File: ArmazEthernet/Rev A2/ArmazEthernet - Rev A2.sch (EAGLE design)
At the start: 114 parts, among them J1 22-05-7028-02, P1 RB1-125BAG1A, U1 LM317MDCY, U2 LM317MDCY, U3 KSZ8995MA, U4 AT24C02C-SSHM-B, X1 NE8FAV, X2 NE8FAV, Y1 8Z-25.000MHZMAAJ-T

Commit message: Update the board with the update schematic
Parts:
- added LED4, LED5, LED6, LED7: Blue, led:LEDCHIP-LED0603
- added R41, R42, R43, R44: 1k, rcl:R-EU_R0603
- JP2, JP3, JP4, JP5: device pinhead:PINHD-1X6 -> pinhead:PINHD-1X8
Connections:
- new net L1-1: JP2.7, JP3.7, R41.2
- new net L1-2: JP2.6, JP3.6, R42.2
- new net L2-1: JP4.7, JP5.7, R43.2
- new net L2-2: JP4.6, JP5.6, R44.2
- new net N$20: LED4.A, R41.1
- new net N$28: LED5.A, R42.1
- new net N$29: LED6.A, R43.1
- new net N$30: LED7.A, R44.1
- net GND: now also JP2.8, JP3.8, JP4.8, JP5.8, LED4.C, LED5.C, LED6.C, LED7.C; no longer JP2.6, JP3.6, JP4.6, JP5.6
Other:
- moved on the sheet: C11, C13, C14, C16, R12, R13, R14, R15, R16, R23, R24, R25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

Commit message: Update board and change NC to DNI
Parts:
- removed R32, R33: 0, NC, rcl:R-EU_R0603
- R30, R31: value 10K -> 10K, DNI
- R35, R36, R37, R38, R39, R40: value 0, NC -> 0, DNI
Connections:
- net N$21 renamed +3V3/FIL
- net N$22 renamed +1V8/FIL
- removed net N$25: R30.1, R32.2
- removed net N$27: R31.1, R33.2
- net L1-1: now also JP2.6, JP3.6, U3B.LED1-0; no longer JP2.7, JP3.7
- net L1-2: now also JP2.7, JP3.7, U3B.LED1-1; no longer JP2.6, JP3.6
- net L2-1: now also JP4.6, JP5.6, U3B.LED2-0; no longer JP4.7, JP5.7
- net L2-2: now also JP4.7, JP5.7, U3B.LED2-1; no longer JP4.6, JP5.6
- net PS0: now also R31.1; no longer R33.1
- net PS1: now also R30.1; no longer R32.1
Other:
- note added: "If CPU Interface controle Mode: Connect R30 Else: Do not connect R30 and R31"
- note removed: "If CPU Interface controle Mode: Connect R32"

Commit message: Update the board
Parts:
- added SJ1: (no value), jumper:SJ
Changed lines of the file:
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@@
 <part name="GND36" library="supply1" deviceset="GND" device=""/>
 <part name="GND37" library="supply1" deviceset="GND" device=""/>
+<part name="SJ1" library="jumper" deviceset="SJ" device=""/>
 </parts>
 <sheets>
@@
 <instance part="GND36" gate="1" x="20.32" y="7.62"/>
 <instance part="GND37" gate="1" x="10.16" y="7.62"/>
+<instance part="SJ1" gate="1" x="63.5" y="167.64"/>
 </instances>
 <busses>

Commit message: Board all route
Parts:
- removed C33: 0.1uF, rcl:C-EUC0603
- removed SJ1: (no value), jumper:SJ
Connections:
- net +1V8: no longer C32.1, C33.1
- net +3V3: now also C32.1
- net GND: no longer C33.2
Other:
- moved on the sheet: C32, C34, C35, C36
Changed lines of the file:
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@@
 <part name="C31" library="rcl" deviceset="C-EU" device="C0603" value="0.1uF"/>
 <part name="C32" library="rcl" deviceset="C-EU" device="C0603" value="0.1uF"/>
-<part name="C33" library="rcl" deviceset="C-EU" device="C0603" value="0.1uF"/>
 <part name="C34" library="rcl" deviceset="C-EU" device="C0603" value="0.1uF"/>
 <part name="C35" library="rcl" deviceset="C-EU" device="C0603" value="0.1uF"/>
@@
 <part name="GND36" library="supply1" deviceset="GND" device=""/>
 <part name="GND37" library="supply1" deviceset="GND" device=""/>
-<part name="SJ1" library="jumper" deviceset="SJ" device=""/>
 </parts>
 <sheets>
@@
 <instance part="GND36" gate="1" x="20.32" y="7.62"/>
 <instance part="GND37" gate="1" x="10.16" y="7.62"/>
-<instance part="SJ1" gate="1" x="63.5" y="167.64"/>
 </instances>
 <busses>
@@
 <text x="358.14" y="246.38" size="1.6764" layer="94">VDDIO</text>
 <text x="335.28" y="246.38" size="1.6764" layer="94">VDDAT</text>
-<text x="335.28" y="220.98" size="1.6764" layer="94">VDDAR</text>
+<text x="342.9" y="220.98" size="1.6764" layer="94">VDDAR</text>
 <text x="358.14" y="198.12" size="1.6764" layer="94">VDDC</text>
 <text x="335.28" y="198.12" size="1.6764" layer="94">VDDAP</text>
@@
 <instance part="C30" gate="G$1" x="340.36" y="241.3"/>
 <instance part="C31" gate="G$1" x="373.38" y="215.9"/>
-<instance part="C32" gate="G$1" x="365.76" y="215.9"/>
-<instance part="C33" gate="G$1" x="358.14" y="215.9"/>
-<instance part="C34" gate="G$1" x="350.52" y="215.9"/>
-<instance part="C35" gate="G$1" x="342.9" y="215.9"/>
-<instance part="C36" gate="G$1" x="335.28" y="215.9"/>
+<instance part="C32" gate="G$1" x="332.74" y="241.3"/>
+<instance part="C34" gate="G$1" x="365.76" y="215.9"/>
+<instance part="C35" gate="G$1" x="358.14" y="215.9"/>
+<instance part="C36" gate="G$1" x="350.52" y="215.9"/>
 <instance part="C37" gate="G$1" x="347.98" y="193.04"/>
 <instance part="C38" gate="G$1" x="373.38" y="193.04"/>
@@
 <wire x1="347.98" y1="236.22" x2="340.36" y2="236.22" width="0.1524" layer="91"/>
 <junction x="347.98" y="236.22"/>
-</segment>
-<segment>
+<pinref part="C32" gate="G$1" pin="2"/>
+<wire x1="340.36" y1="236.22" x2="332.74" y2="236.22" width="0.1524" layer="91"/>
+<junction x="340.36" y="236.22"/>
+</segment>
+<segment>
+<pinref part="C31" gate="G$1" pin="2"/>
 <pinref part="GND24" gate="1" pin="GND"/>
-<pinref part="C31" gate="G$1" pin="2"/>
 <wire x1="373.38" y1="208.28" x2="373.38" y2="210.82" width="0.1524" layer="91"/>
-<pinref part="C32" gate="G$1" pin="2"/>
-<wire x1="373.38" y1="210.82" x2="365.76" y2="210.82" width="0.1524" layer="91"/>
+<pinref part="C36" gate="G$1" pin="2"/>
+<pinref part="C35" gate="G$1" pin="2"/>
+<junction x="358.14" y="210.82"/>
+<wire x1="365.76" y1="210.82" x2="358.14" y2="210.82" width="0.1524" layer="91"/>
+<wire x1="358.14" y1="210.82" x2="350.52" y2="210.82" width="0.1524" layer="91"/>
+<pinref part="C34" gate="G$1" pin="2"/>
+<junction x="365.76" y="210.82"/>
+<wire x1="365.76" y1="210.82" x2="373.38" y2="210.82" width="0.1524" layer="91"/>
 <junction x="373.38" y="210.82"/>
-<pinref part="C33" gate="G$1" pin="2"/>
-<wire x1="365.76" y1="210.82" x2="358.14" y2="210.82" width="0.1524" layer="91"/>
-<junction x="365.76" y="210.82"/>
-<pinref part="C36" gate="G$1" pin="2"/>
-<wire x1="358.14" y1="210.82" x2="350.52" y2="210.82" width="0.1524" layer="91"/>
-<junction x="358.14" y="210.82"/>
-<pinref part="C35" gate="G$1" pin="2"/>
-<junction x="342.9" y="210.82"/>
-<wire x1="350.52" y1="210.82" x2="342.9" y2="210.82" width="0.1524" layer="91"/>
-<wire x1="342.9" y1="210.82" x2="335.28" y2="210.82" width="0.1524" layer="91"/>
-<pinref part="C34" gate="G$1" pin="2"/>
-<junction x="350.52" y="210.82"/>
 </segment>
 <segment>
@@
 <wire x1="347.98" y1="243.84" x2="347.98" y2="246.38" width="0.1524" layer="91"/>
 <junction x="347.98" y="243.84"/>
+<pinref part="C32" gate="G$1" pin="1"/>
+<wire x1="340.36" y1="243.84" x2="332.74" y2="243.84" width="0.1524" layer="91"/>
+<junction x="340.36" y="243.84"/>
 </segment>
 <segment>
@@
 <pinref part="C36" gate="G$1" pin="1"/>
 <pinref part="C35" gate="G$1" pin="1"/>
-<wire x1="335.28" y1="218.44" x2="342.9" y2="218.44" width="0.1524" layer="91"/>
+<wire x1="350.52" y1="218.44" x2="358.14" y2="218.44" width="0.1524" layer="91"/>
 <pinref part="C34" gate="G$1" pin="1"/>
-<wire x1="342.9" y1="218.44" x2="350.52" y2="218.44" width="0.1524" layer="91"/>
-<junction x="342.9" y="218.44"/>
-<pinref part="C33" gate="G$1" pin="1"/>
-<wire x1="350.52" y1="218.44" x2="358.14" y2="218.44" width="0.1524" layer="91"/>
-<junction x="350.52" y="218.44"/>
-<pinref part="C32" gate="G$1" pin="1"/>
 <wire x1="358.14" y1="218.44" x2="365.76" y2="218.44" width="0.1524" layer="91"/>
 <junction x="358.14" y="218.44"/>
-<pinref part="C31" gate="G$1" pin="1"/>
-<wire x1="365.76" y1="218.44" x2="373.38" y2="218.44" width="0.1524" layer="91"/>
-<junction x="365.76" y="218.44"/>
-<wire x1="373.38" y1="218.44" x2="373.38" y2="220.98" width="0.1524" layer="91"/>
-<junction x="373.38" y="218.44"/>
-<pinref part="+1V6" gate="G$1" pin="+3V3"/>
 </segment>
 <segment>
@@
 <pinref part="+1V8" gate="G$1" pin="+3V3"/>
 </segment>
-</net>
+<segment>
+<pinref part="+1V6" gate="G$1" pin="+3V3"/>
+<pinref part="C31" gate="G$1" pin="1"/>
+<wire x1="373.38" y1="218.44" x2="373.38" y2="220.98" width="0.1524" layer="91"/>
+<wire x1="365.76" y1="218.44" x2="373.38" y2="218.44" width="0.1524" layer="91"/>
+<junction x="373.38" y="218.44"/>
+</segment>
+</net>

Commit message: Update board
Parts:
- added C33, C44: 0.1uF, rcl:C-EUC0603
- added R32, R33, R45, R46: 49.9, rcl:R-EU_R0603
- added U$5, U$8: EXMACHINA-LOGO-NAME, exmachina:EXMACHINA-LOGO-NAME
- added U$6, U$7: CC-BY-SA, cc-by-sa:CC-BY-SA
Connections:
- net RX1+ renamed RX1_P
- net RX1- renamed RX1_M
- net RX1M_ISO renamed RX1_ISO_M
- net RX1P_ISO renamed RX1_ISO_P
- net RX2+ renamed RX2_P
- net RX2- renamed RX2_M
- net RX2M_ISO renamed RX2_ISO_M
- net RX2P_ISO renamed RX2_ISO_P
- net TX1+ renamed TX1_P
- net TX1- renamed TX1_M
- net TX1M_ISO renamed TX1_ISO_M
- net TX1P_ISO renamed TX1_ISO_P
- net TX2+ renamed TX2_P
- net TX2- renamed TX2_M
- net TX2M_ISO renamed TX2_ISO_M
- net TX2P_ISO renamed TX2_ISO_P
- removed net RX3M_ISO: P1.RD-, U3A.RXM3
- removed net RX3P_ISO: P1.RD+, U3A.RXP3
- removed net TX3M_ISO: P1.TD-, U3A.TXM3
- removed net TX3P_ISO: P1.TD+, U3A.TXP3
- new net N$27: C33.1, R32.1, R33.1
- new net N$31: C44.1, R45.1, R46.1
- new net RX3_ISO_M: P1.RD-, R46.2, U3A.RXM3
- new net RX3_ISO_P: P1.RD+, R45.2, U3A.RXP3
- new net TX3_ISO_M: P1.TD-, R33.2, U3A.TXM3
- new net TX3_ISO_P: P1.TD+, R32.2, U3A.TXP3
- net GND: now also C33.2, C44.2

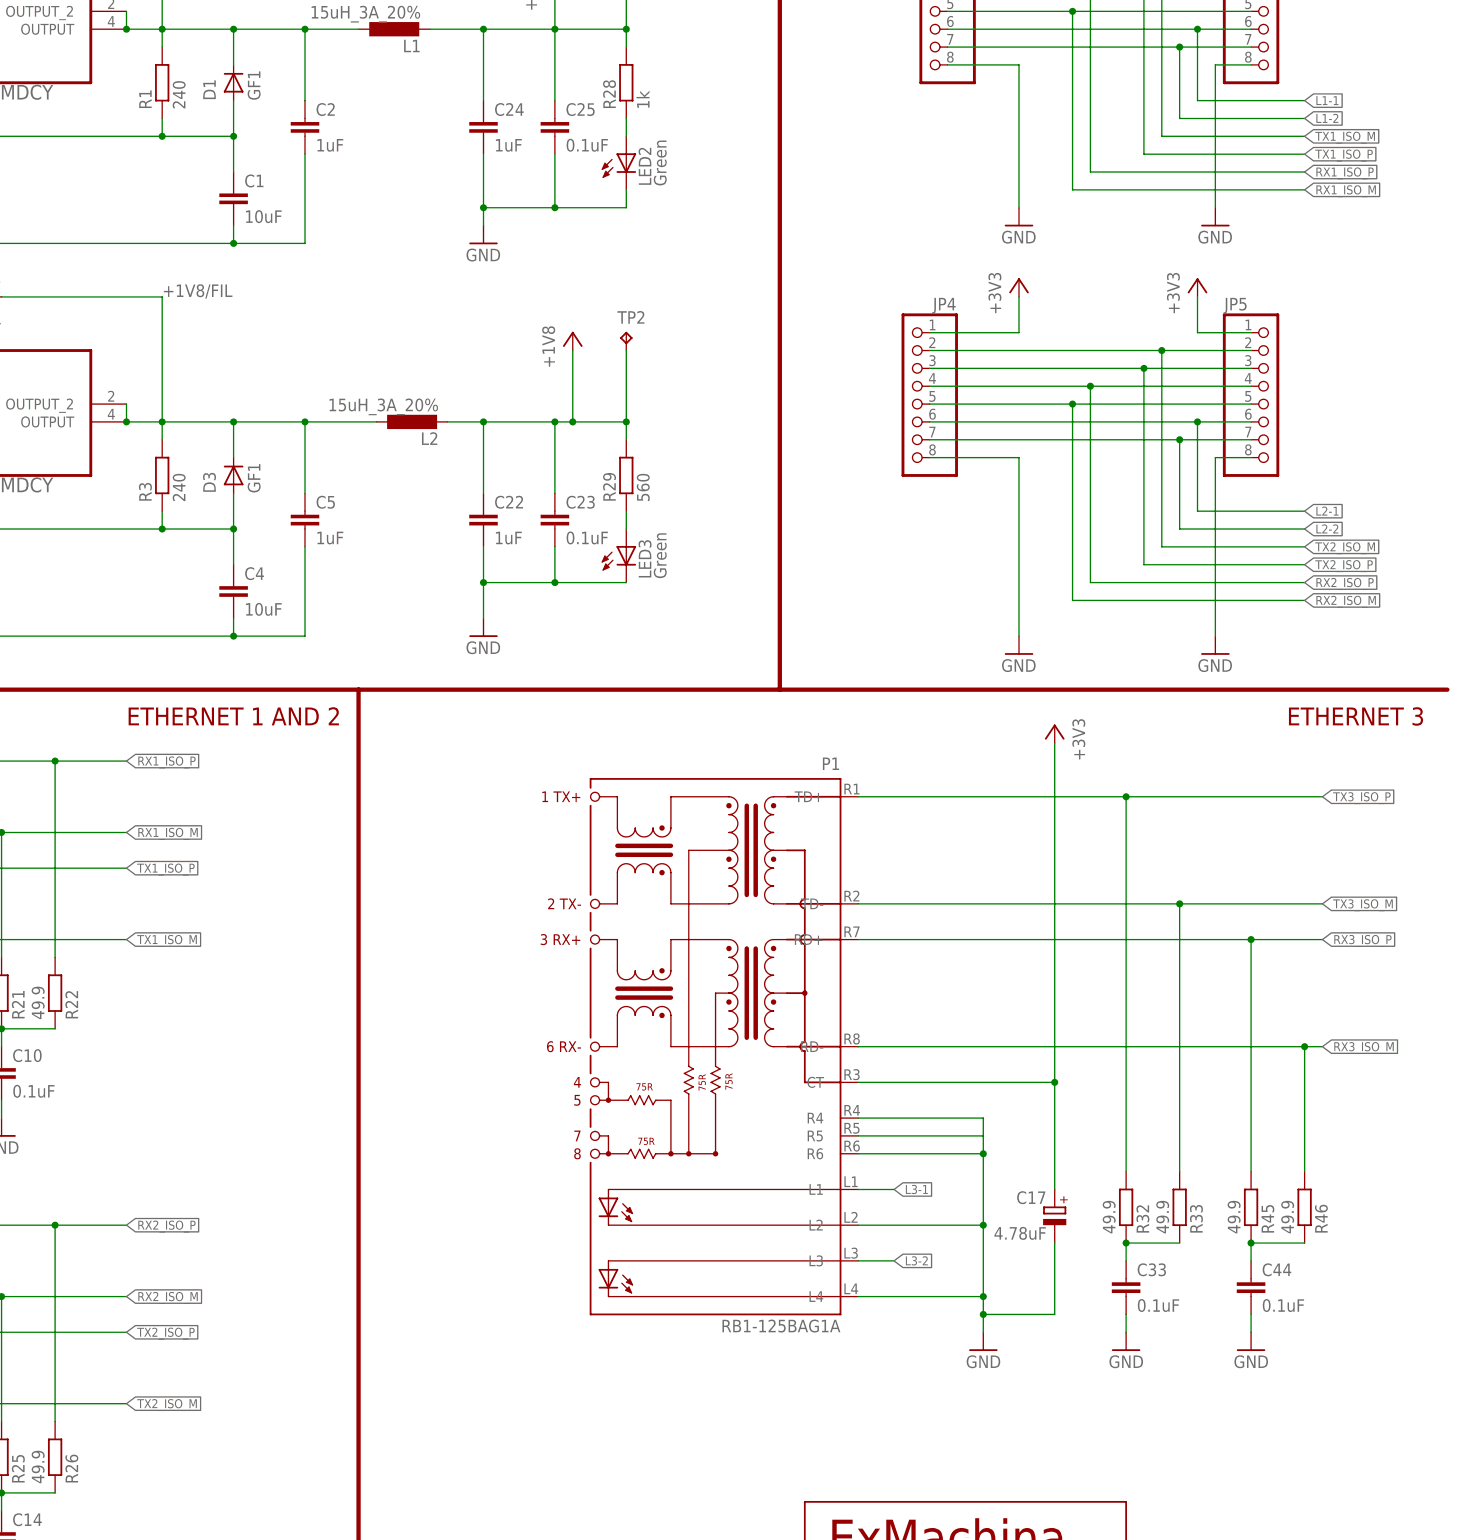
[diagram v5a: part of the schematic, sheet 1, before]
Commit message: Turn JP2 Add res to L3 Add reset circuit Add rev to the silkscreen Add Keepout near the transfo
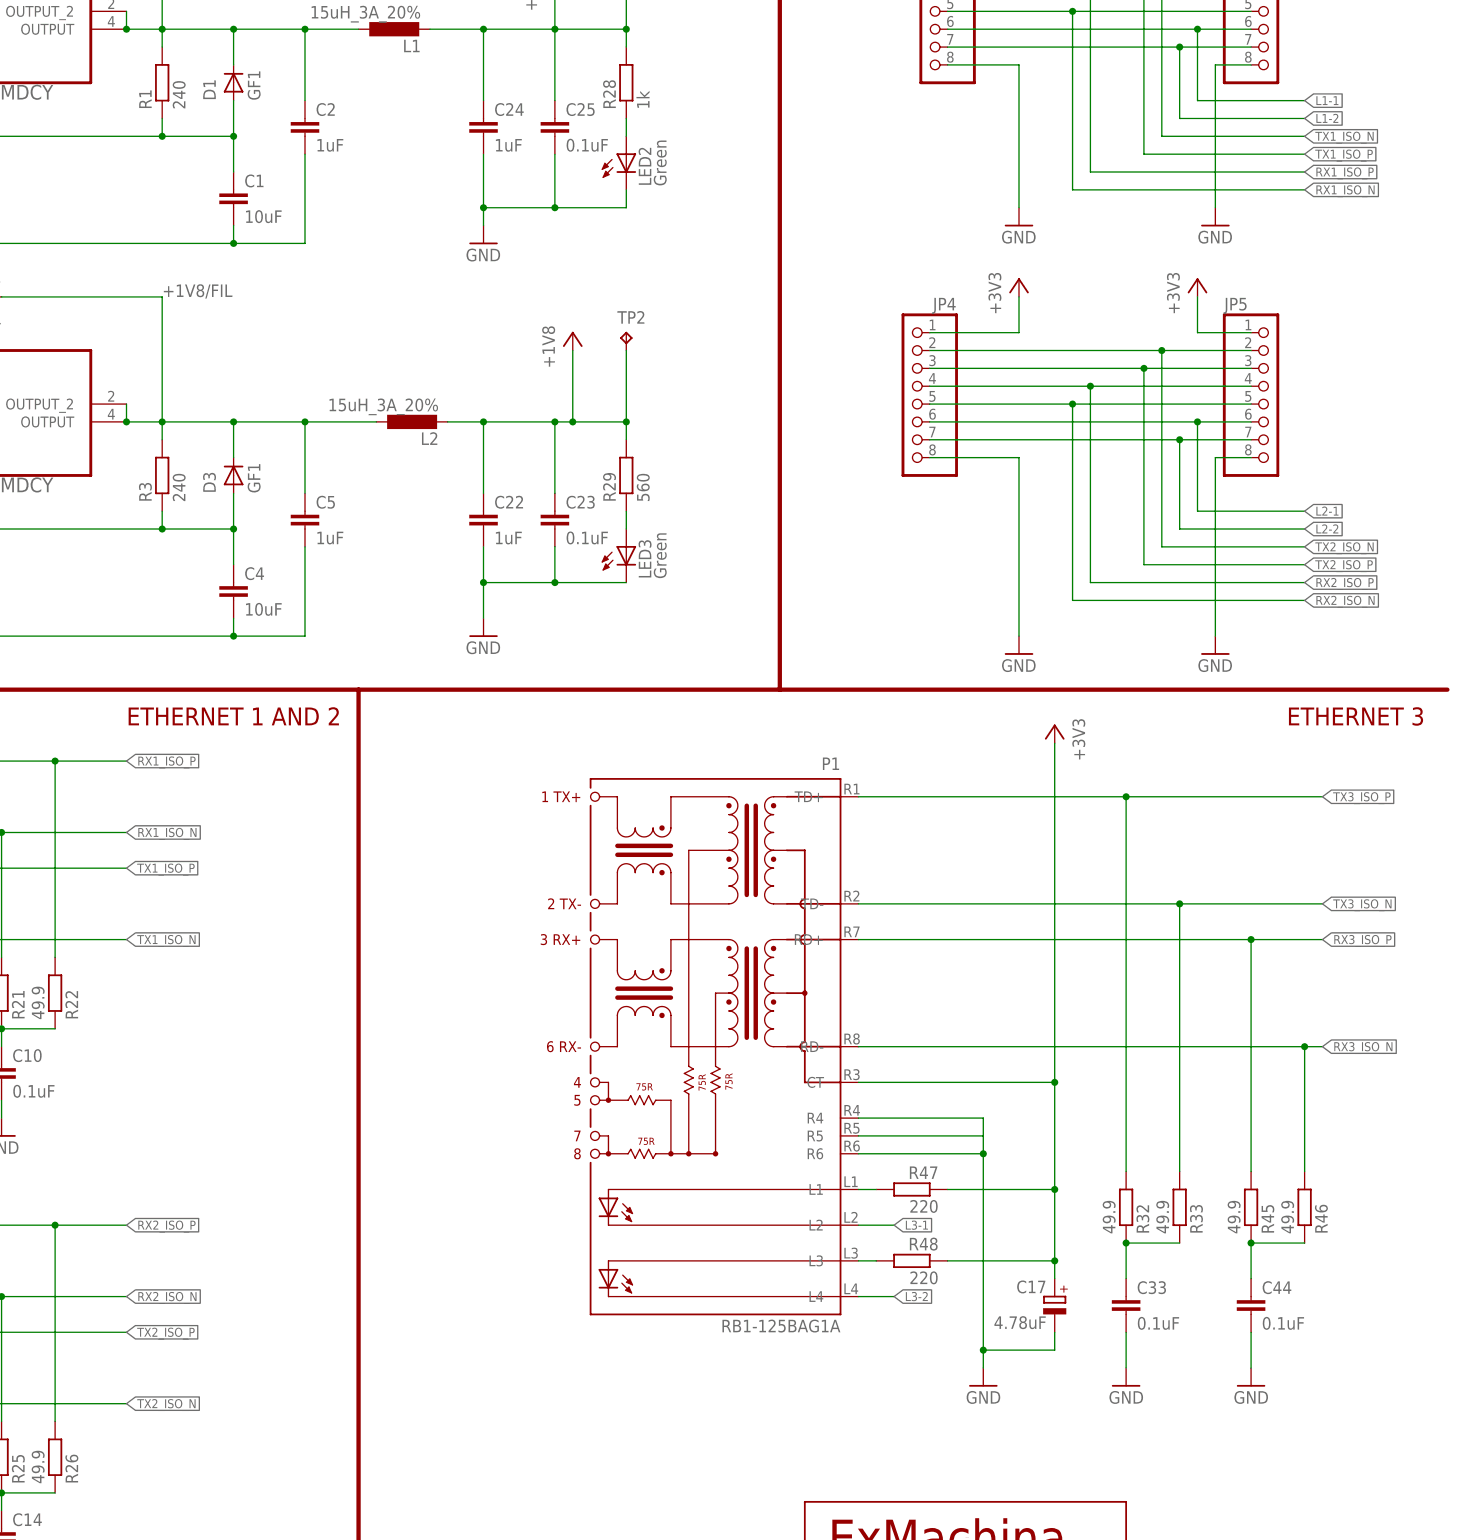
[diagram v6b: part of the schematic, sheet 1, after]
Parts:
- removed U$7: CC-BY-SA, cc-by-sa:CC-BY-SA
- added C45: 10uF, rcl:C-EUC0603
- added R47, R48: 220, rcl:R-EU_R0603
- added R49: 10K, rcl:R-EU_R0603
- added U$9: 1N4148W, diode:1N4148W
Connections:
- net RX1_ISO_M renamed RX1_ISO_N
- net RX2_ISO_M renamed RX2_ISO_N
- net RX3_ISO_M renamed RX3_ISO_N
- net TX1_ISO_M renamed TX1_ISO_N
- net TX2_ISO_M renamed TX2_ISO_N
- net TX3_ISO_M renamed TX3_ISO_N
- new net N$34: P1.L3, R48.2
- new net N$35: P1.L1, R47.2
- net +3V3: now also R47.1, R48.1, R49.2, U$9.1
- net GND: now also C45.2; no longer P1.L2, P1.L4
- net L3-1: now also P1.L2; no longer P1.L1
- net L3-2: now also P1.L4; no longer P1.L3
- net RST_N: now also C45.1, R49.1, U$9.2
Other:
- note added: "RESET"
- moved on the sheet: C17, C33, C44

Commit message: Add condos between the ground of NE8FAV and the gnd
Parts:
- added C46, C47: 1000pF, 2kV, rcl:C-EUC1206
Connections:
- new net N$36: C47.1, X2.G
- new net N$37: C46.1, X1.G
- net GND: now also C46.2, C47.2
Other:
- note added: "LED ETHERNET"
- note removed: "ETHERNET 1 AND 2"
- moved on the sheet: C17, C33, C44, LED4, LED5, LED6, LED7, P1, R32, R33, R41, R42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
